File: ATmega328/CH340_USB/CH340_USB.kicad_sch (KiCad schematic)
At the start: 28 parts, among them J1 USB_C Conn, SW1 RESET, U1 ATMEGA328P-PU, U2 CH340C, Y1 16MHz, Y2 12MHz

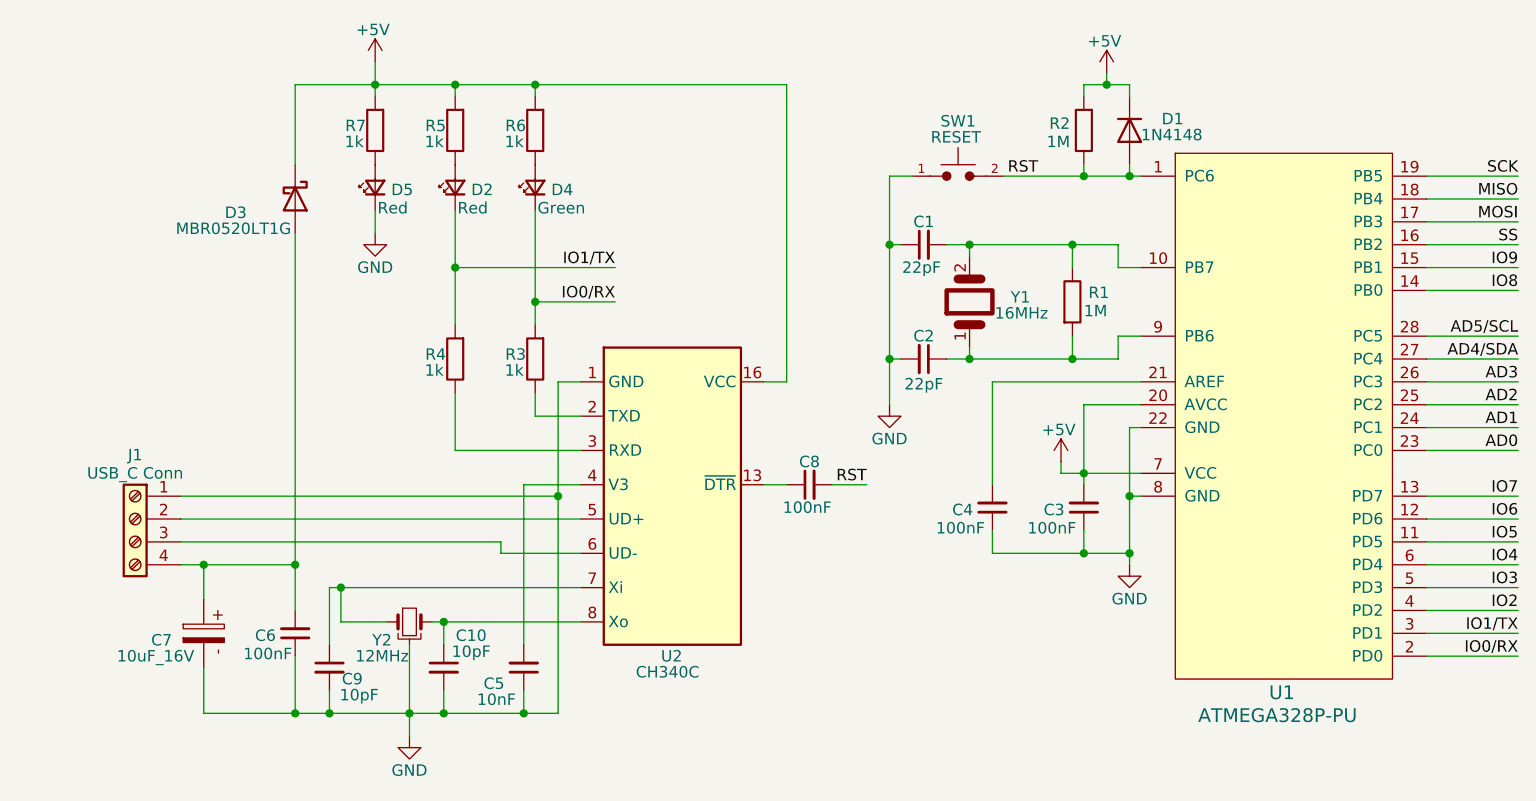
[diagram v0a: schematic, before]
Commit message: The CH340C was changed to CH340G
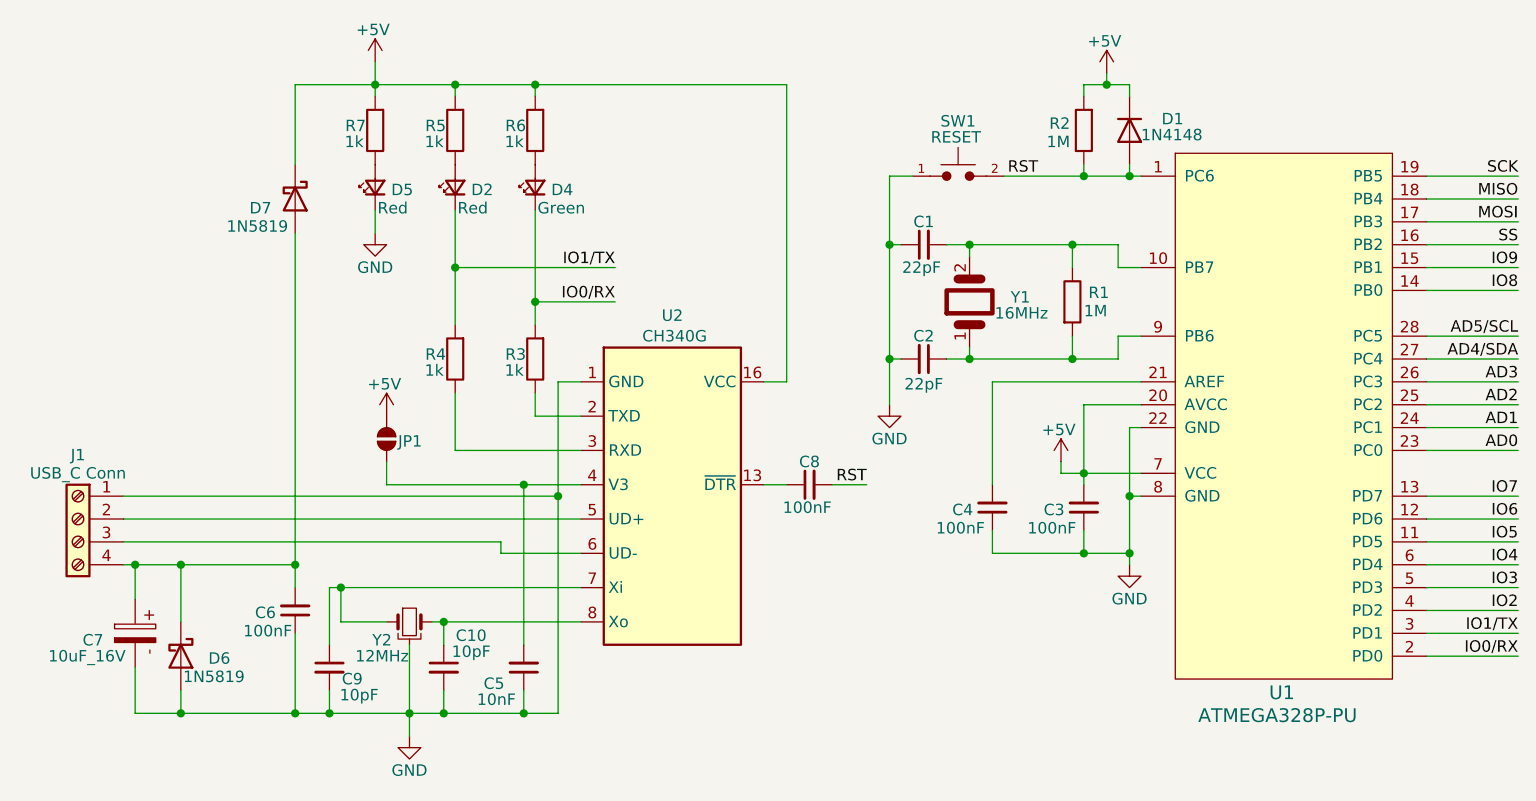
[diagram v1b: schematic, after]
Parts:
- removed D3: MBR0520LT1G, Diode_THT:D_DO-201AD_P15.24mm_Horizontal, symbol Diode:1N5822
- added D6, D7: 1N5819, Diode_THT:D_DO-41_SOD81_P10.16mm_Horizontal, symbol Diode:1N5819
- added JP1: ~, SparkFun-Jumper:Jumper_2_NO, symbol SparkFun-Jumper:SolderJumper_2_Open
- U2: value CH340C -> CH340G
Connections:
- net +5V: now also D7.1 (K), JP1.2 (B)
- net GND: now also D6.2 (A)
- net at C5.2, U2.4 (V3): now also JP1.1 (A)
- net at C6.2, C7.1, J1.4 (Pin_4): now also D6.1 (K), D7.2 (A)
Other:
- moved on the sheet: C6, C7, J1
